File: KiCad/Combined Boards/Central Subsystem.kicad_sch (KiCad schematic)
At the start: 39 parts, among them J1 Antenna, J1 Sensor Subsystem, J2 Debug, J3 LoRa Debug, Q1 SI2301CDS-T1-GE3, U1 STM32WLE5CCU6, Y1 32 MHz

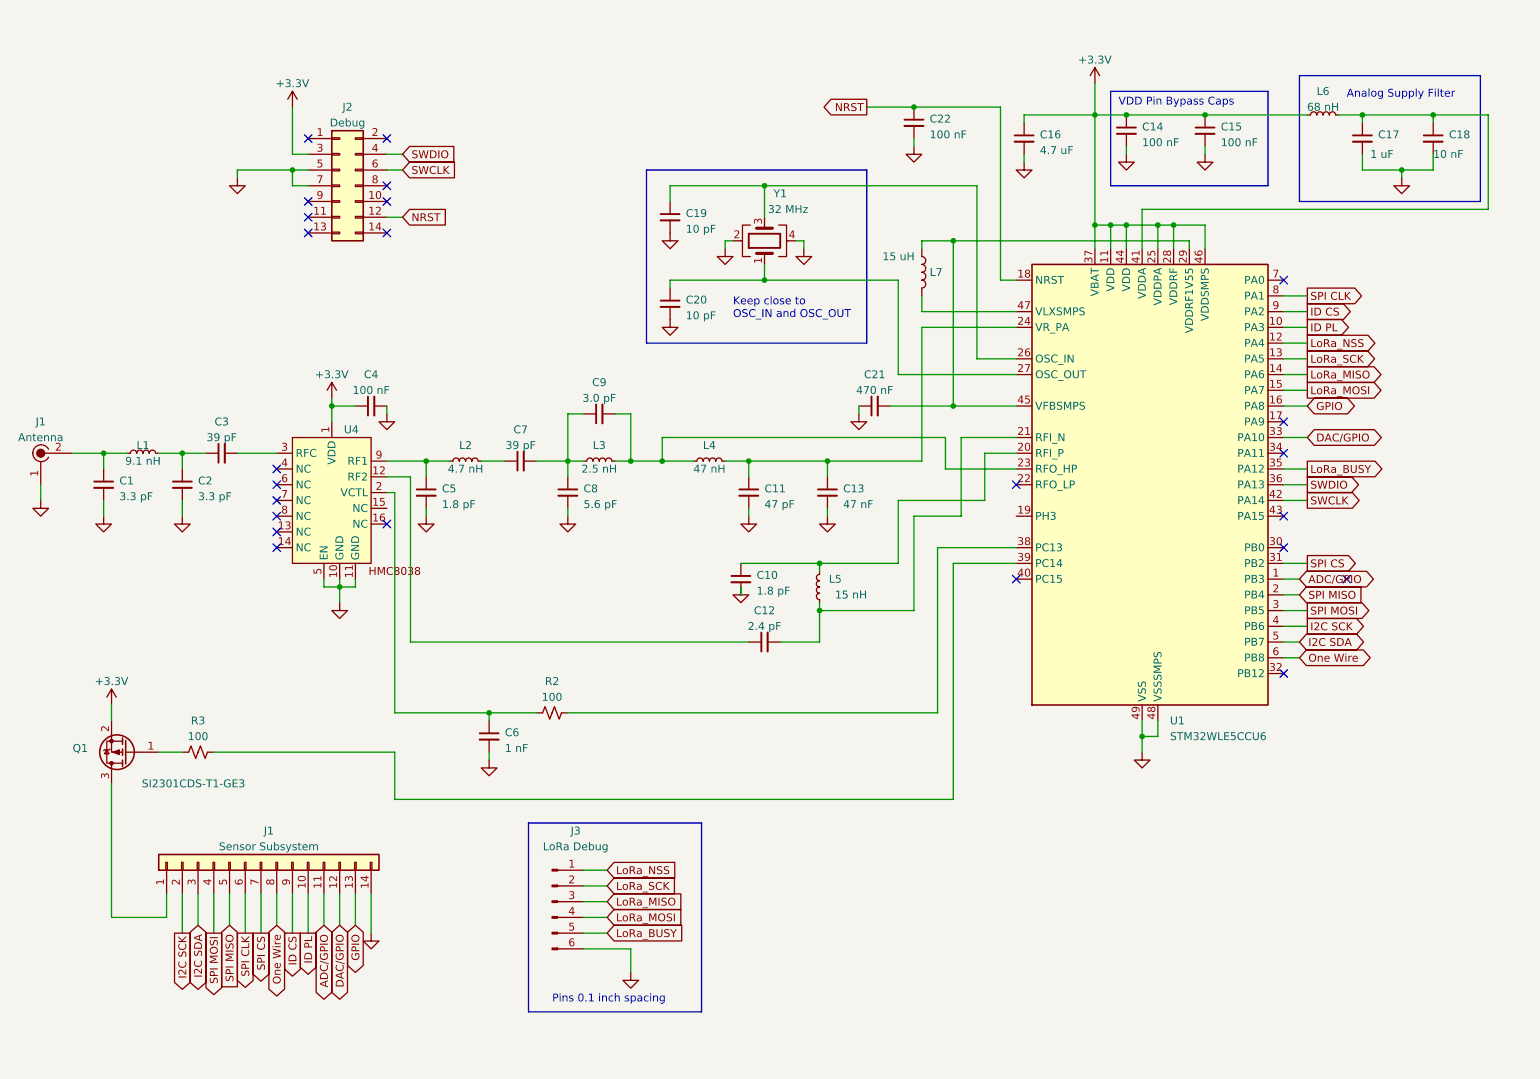
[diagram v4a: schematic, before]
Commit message: Updated combined board schematics
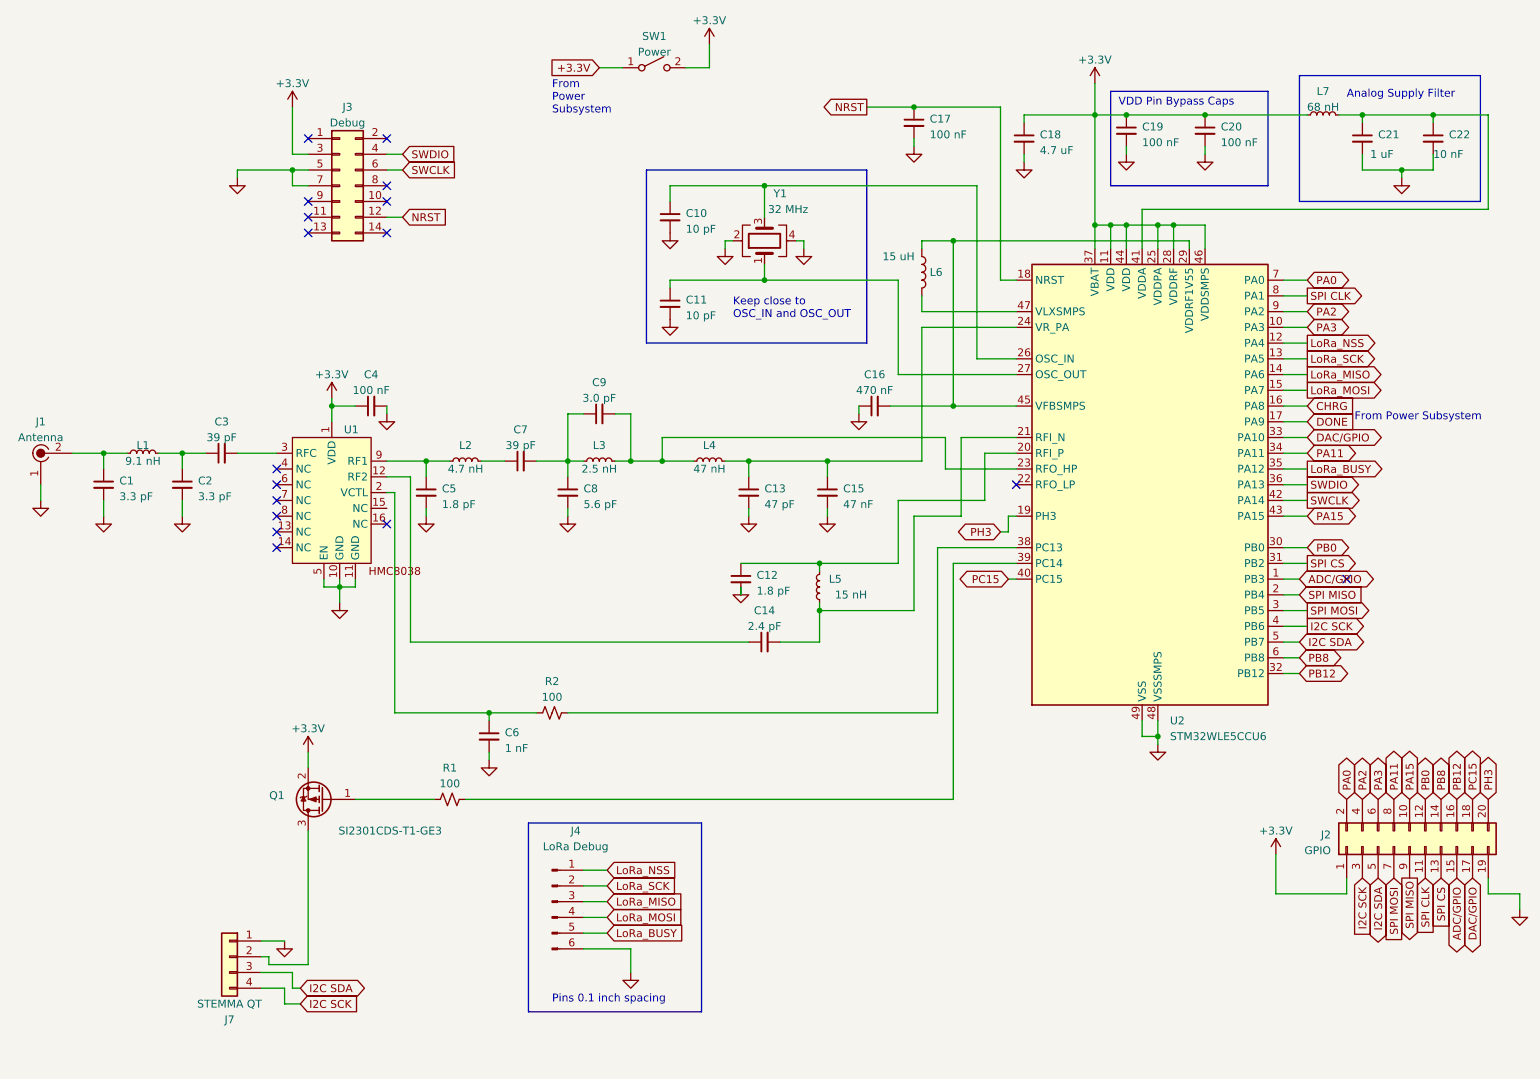
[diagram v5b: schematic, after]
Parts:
- removed J1: Sensor Subsystem, symbol Connector_Generic:Conn_01x14
- added J2: GPIO, symbol Connector_Generic:Conn_02x10_Odd_Even
- added J7: STEMMA QT, symbol Connector_Generic:Conn_01x04
- added SW1: Power, symbol Switch:SW_SPST
- renumbered C19 to C10, C20 to C11, C10 to C12, C11 to C13, C12 to C14, C13 to C15, C21 to C16, C22 to C17, C16 to C18, C14 to C19, C15 to C20, C17 to C21, C18 to C22, J2 to J3, J3 to J4, L7 to L6, L6 to L7, R3 to R1, U4 to U1, U1 to U2
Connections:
- net +3.3V: now also J2.1 (Pin_1), SW1.1 (A), SW1.2 (B)
- net ADC/GPIO: now also J2.15 (Pin_15)
- net DAC/GPIO: now also J2.17 (Pin_17)
- net GND: now also J2.19 (Pin_19), J7.1 (Pin_1)
- net I2C SCK: now also J2.3 (Pin_3), J7.4 (Pin_4)
- net I2C SDA: now also J2.5 (Pin_5), J7.3 (Pin_3)
- net SPI CLK: now also J2.11 (Pin_11)
- net SPI CS: now also J2.13 (Pin_13)
- net SPI MISO: now also J2.9 (Pin_9)
- net SPI MOSI: now also J2.7 (Pin_7)
- net at Q1.3 (D): now also J7.2 (Pin_2)
- net DONE: now reaches U2.17 (PA9)
- net PH3: now reaches U2.19 (PH3)
- net PH3: now also J2.20 (Pin_20)
- net PB0: now reaches U2.30 (PB0)
- net PB0: now also J2.12 (Pin_12)
- net PB12: now reaches U2.32 (PB12)
- net PB12: now also J2.16 (Pin_16)
- net PA11: now reaches U2.34 (PA11)
- net PA11: now also J2.8 (Pin_8)
- net PC15: now reaches U2.40 (PC15)
- net PC15: now also J2.18 (Pin_18)
- net PA15: now reaches U2.43 (PA15)
- net PA15: now also J2.10 (Pin_10)
- net PA0: now reaches U2.7 (PA0)
- net PA0: now also J2.2 (Pin_2)
- net GPIO renamed CHRG
- net ID CS renamed PA2
- net PA2: now also J2.4 (Pin_4)
- net ID PL renamed PA3
- net PA3: now also J2.6 (Pin_6)
- net One Wire renamed PB8
- net PB8: now also J2.14 (Pin_14)
- no-connect marks 24 -> 17
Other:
- note added: "From Power Subsystem"
- moved on the sheet: Q1, R1

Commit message: Updated combined board schematic
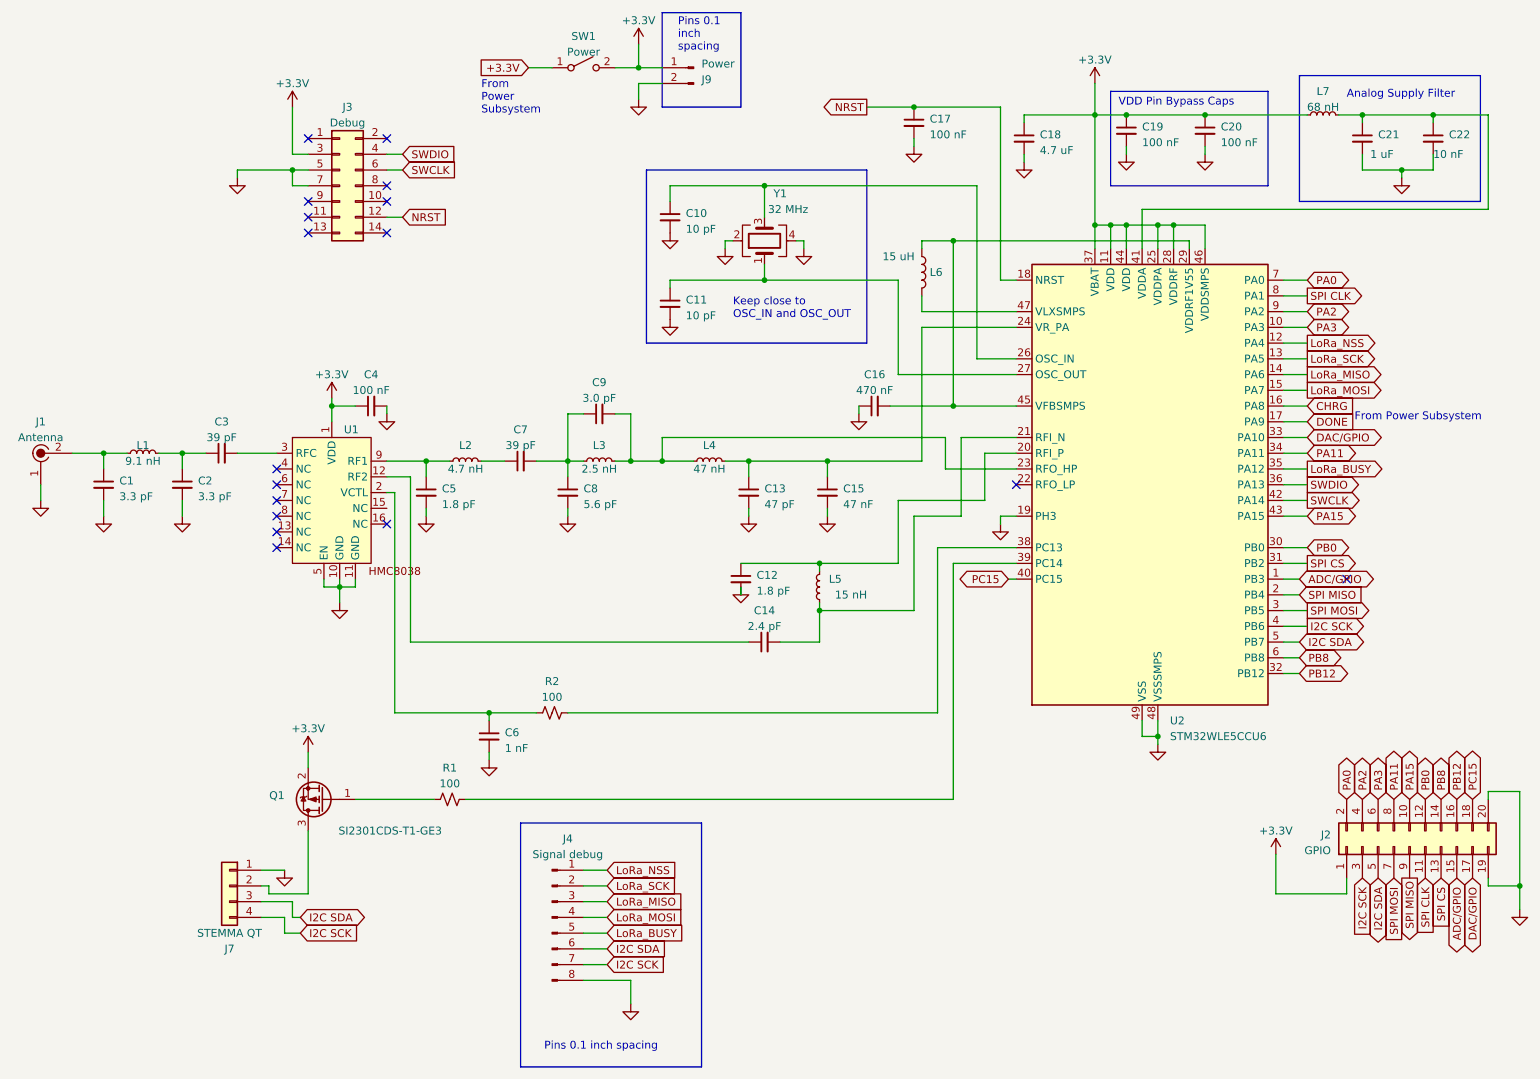
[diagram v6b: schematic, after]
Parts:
- removed J4: LoRa Debug, symbol Connector:Conn_01x06_Pin
- added J4: Signal debug, symbol Connector:Conn_01x08_Pin
- added J9: Power, symbol Connector:Conn_01x02_Pin
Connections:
- net PH3 is gone; now on net GND: J2.20 (Pin_20), U2.19 (PH3)
- net +3.3V: now also J9.1 (Pin_1)
- net GND: now also J4.8 (Pin_8), J9.2 (Pin_2)
- net I2C SCK: now also J4.7 (Pin_7)
- net I2C SDA: now also J4.6 (Pin_6)
- net LoRa_BUSY: now also J4.5 (Pin_5)
- net LoRa_MISO: now also J4.3 (Pin_3)
- net LoRa_MOSI: now also J4.4 (Pin_4)
- net LoRa_NSS: now also J4.1 (Pin_1)
- net LoRa_SCK: now also J4.2 (Pin_2)
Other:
- moved on the sheet: J7, SW1

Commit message: Include UART pins
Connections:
- net PA2 renamed  LPUART TX
- net  LPUART TX: no longer J2.4 (Pin_4)
- net PA3 renamed LPUART RX
- new net LPUART TX: J2.4 (Pin_4)
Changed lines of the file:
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@@
     )
   )
-  (global_label "PA3" (shape bidirectional) (at 223.52 68.58 0) (fields_autoplaced)
+  (global_label "LPUART RX" (shape input) (at 223.52 68.58 0) (fields_autoplaced)
     (effects (font (size 1.27 1.27)) (justify left))
-    (property "Intersheetrefs" "${INTERSHEET_REFS}" (at 231.1052 68.58 0)
+    (property "Intersheetrefs" "${INTERSHEET_REFS}" (at 236.8277 68.58 0)
       (effects (font (size 1.27 1.27)) (justify left) hide)
     )
@@
     )
   )
-  (global_label "PA3" (shape bidirectional) (at 234.95 144.78 90) (fields_autoplaced)
+  (global_label "LPUART RX" (shape output) (at 234.95 144.78 90) (fields_autoplaced)
     (effects (font (size 1.27 1.27)) (justify left))
-    (property "Intersheetrefs" "${INTERSHEET_REFS}" (at 234.95 137.1948 90)
+    (property "Intersheetrefs" "${INTERSHEET_REFS}" (at 234.95 131.4723 90)
       (effects (font (size 1.27 1.27)) (justify left) hide)
     )
@@
     )
   )
-  (global_label "PA2" (shape bidirectional) (at 232.41 144.78 90) (fields_autoplaced)
+  (global_label "LPUART TX" (shape input) (at 232.41 144.78 90) (fields_autoplaced)
     (effects (font (size 1.27 1.27)) (justify left))
-    (property "Intersheetrefs" "${INTERSHEET_REFS}" (at 232.41 137.1948 90)
+    (property "Intersheetrefs" "${INTERSHEET_REFS}" (at 232.41 131.7747 90)
       (effects (font (size 1.27 1.27)) (justify left) hide)
     )
@@
     )
   )
-  (global_label "PA2" (shape bidirectional) (at 223.52 66.04 0) (fields_autoplaced)
+  (global_label " LPUART TX" (shape output) (at 223.52 66.04 0) (fields_autoplaced)
     (effects (font (size 1.27 1.27)) (justify left))
-    (property "Intersheetrefs" "${INTERSHEET_REFS}" (at 231.1052 66.04 0)
+    (property "Intersheetrefs" "${INTERSHEET_REFS}" (at 237.4929 66.04 0)
       (effects (font (size 1.27 1.27)) (justify left) hide)
     )

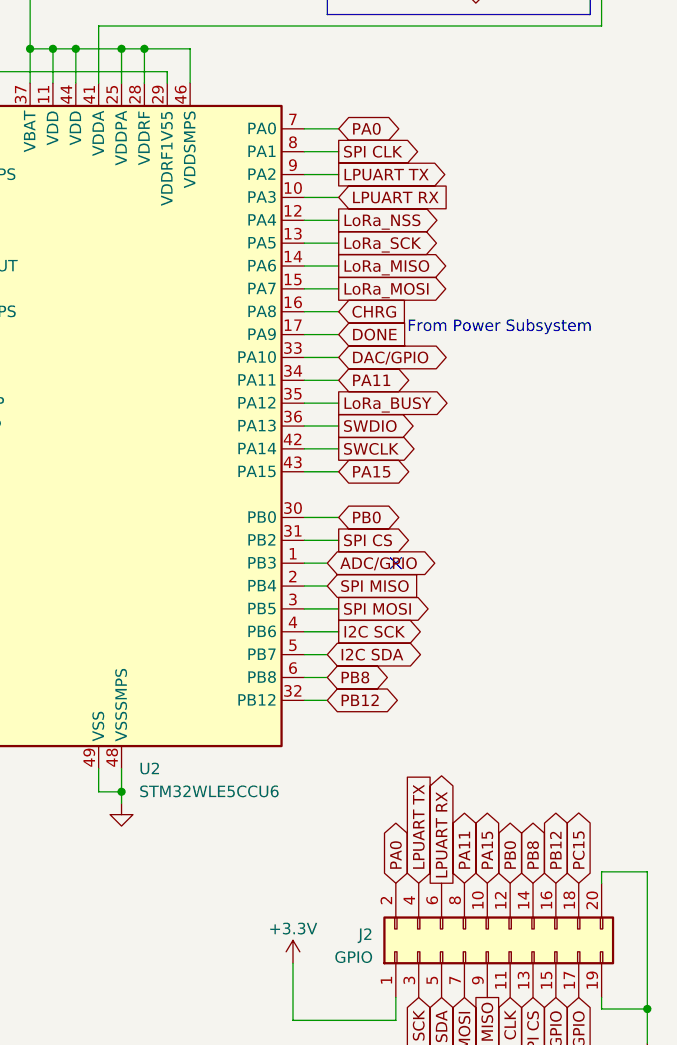
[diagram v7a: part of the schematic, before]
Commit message: Update UART pin labels
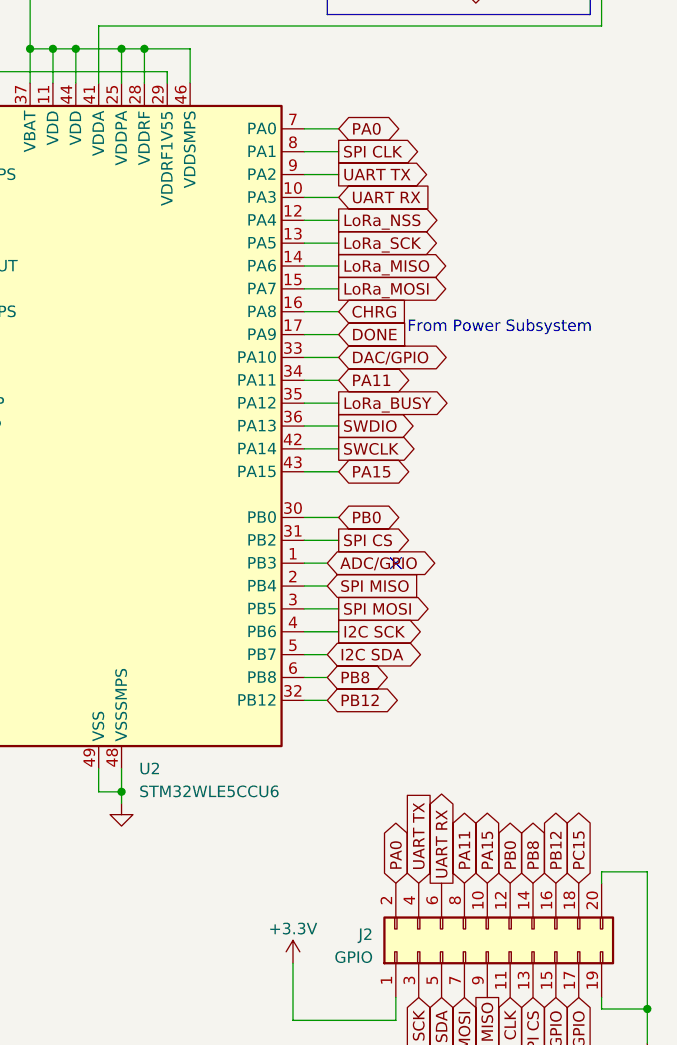
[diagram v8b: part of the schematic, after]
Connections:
- net  LPUART TX renamed  UART TX
- net LPUART RX renamed UART RX
- net LPUART TX renamed UART TX
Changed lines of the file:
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@@
     )
   )
-  (global_label "LPUART RX" (shape input) (at 223.52 68.58 0) (fields_autoplaced)
+  (global_label "UART RX" (shape input) (at 223.52 68.58 0) (fields_autoplaced)
     (effects (font (size 1.27 1.27)) (justify left))
-    (property "Intersheetrefs" "${INTERSHEET_REFS}" (at 236.8277 68.58 0)
+    (property "Intersheetrefs" "${INTERSHEET_REFS}" (at 234.5296 68.58 0)
       (effects (font (size 1.27 1.27)) (justify left) hide)
     )
@@
     )
   )
-  (global_label "LPUART RX" (shape output) (at 234.95 144.78 90) (fields_autoplaced)
+  (global_label "UART RX" (shape output) (at 234.95 144.78 90) (fields_autoplaced)
     (effects (font (size 1.27 1.27)) (justify left))
-    (property "Intersheetrefs" "${INTERSHEET_REFS}" (at 234.95 131.4723 90)
+    (property "Intersheetrefs" "${INTERSHEET_REFS}" (at 234.95 133.7704 90)
       (effects (font (size 1.27 1.27)) (justify left) hide)
     )
@@
     )
   )
-  (global_label "LPUART TX" (shape input) (at 232.41 144.78 90) (fields_autoplaced)
+  (global_label "UART TX" (shape input) (at 232.41 144.78 90) (fields_autoplaced)
     (effects (font (size 1.27 1.27)) (justify left))
-    (property "Intersheetrefs" "${INTERSHEET_REFS}" (at 232.41 131.7747 90)
+    (property "Intersheetrefs" "${INTERSHEET_REFS}" (at 232.41 134.0728 90)
       (effects (font (size 1.27 1.27)) (justify left) hide)
     )
@@
     )
   )
-  (global_label " LPUART TX" (shape output) (at 223.52 66.04 0) (fields_autoplaced)
+  (global_label " UART TX" (shape output) (at 223.52 66.04 0) (fields_autoplaced)
     (effects (font (size 1.27 1.27)) (justify left))
-    (property "Intersheetrefs" "${INTERSHEET_REFS}" (at 237.4929 66.04 0)
+    (property "Intersheetrefs" "${INTERSHEET_REFS}" (at 235.1948 66.04 0)
       (effects (font (size 1.27 1.27)) (justify left) hide)
     )
